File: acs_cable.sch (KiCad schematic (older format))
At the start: 0 parts

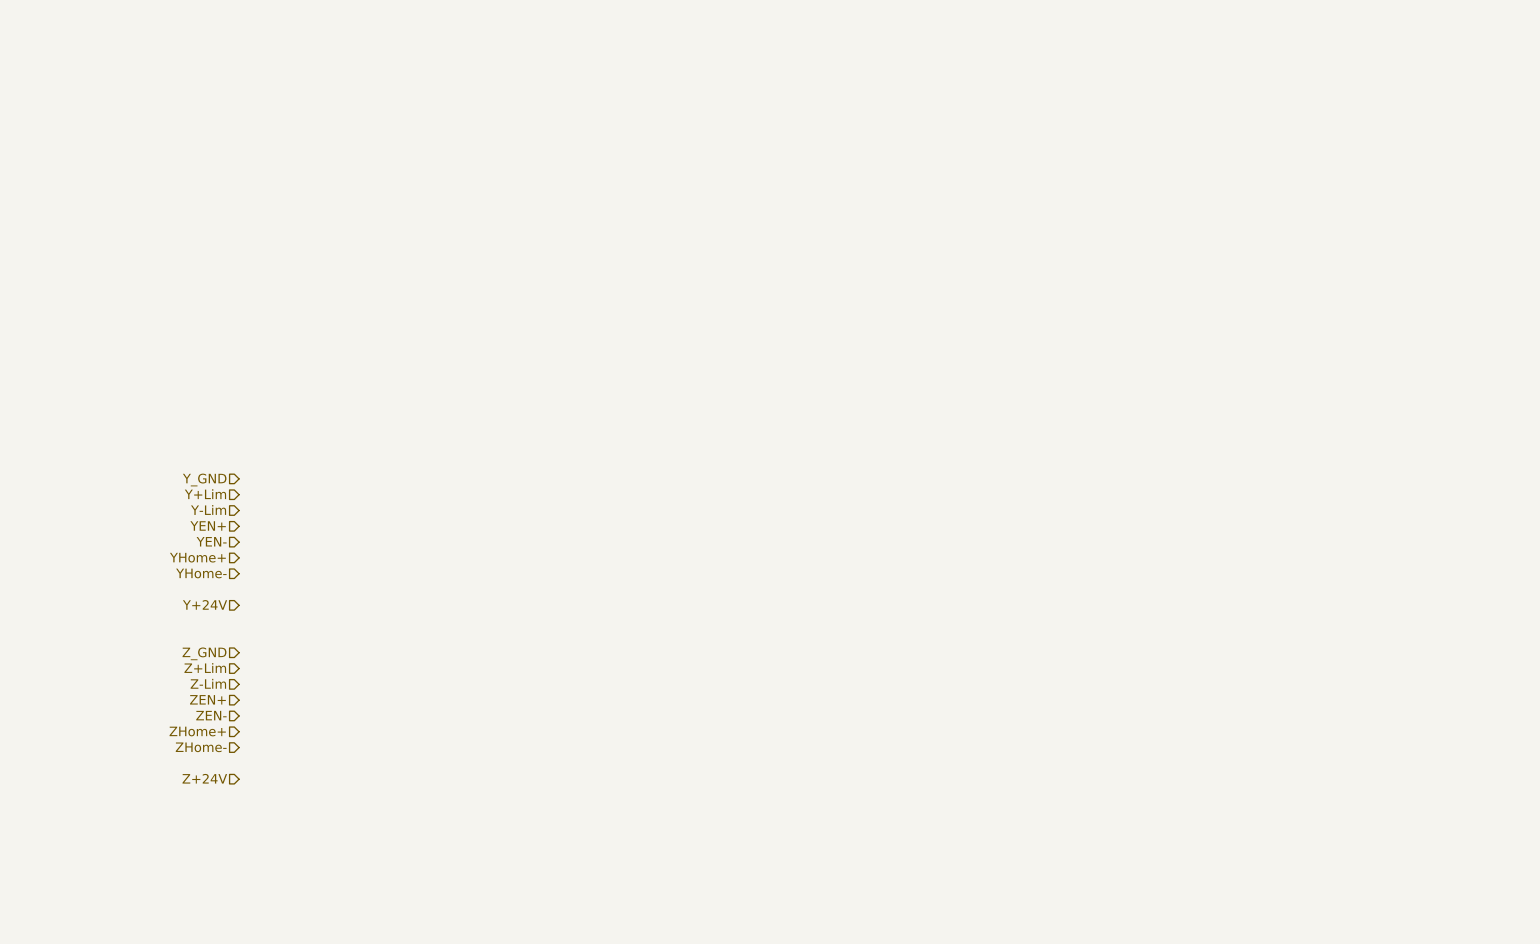
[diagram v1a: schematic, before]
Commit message: set limits to pull down, optional invert
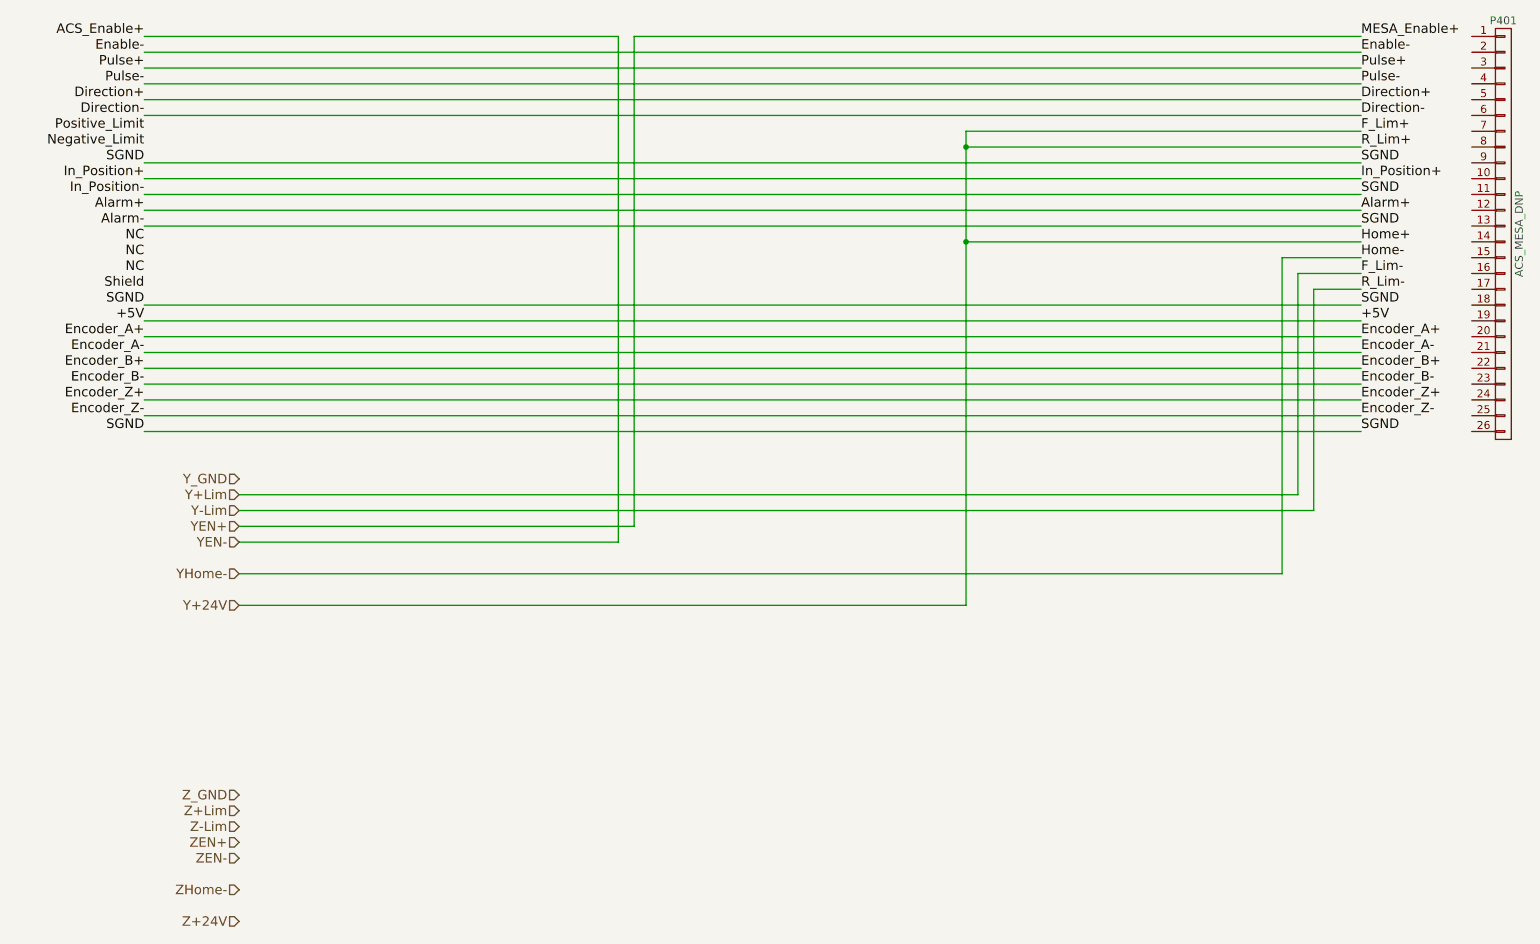
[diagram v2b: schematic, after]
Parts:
- added P401: ACS_MESA_DNP, symbol CONN_01X26
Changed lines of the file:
@@
 Text HLabel 2600 4400 0    60   Input ~ 0
 YEN-
-Text HLabel 2600 4500 0    60   Input ~ 0
-YHome+
 Text HLabel 2600 4600 0    60   Input ~ 0
 YHome-
 Text HLabel 2600 4800 0    60   Input ~ 0
 Y+24V
-Text HLabel 2600 5100 0    60   Input ~ 0
+Text HLabel 2600 6000 0    60   Input ~ 0
 Z_GND
-Text HLabel 2600 5200 0    60   Input ~ 0
+Text HLabel 2600 6100 0    60   Input ~ 0
 Z+Lim
-Text HLabel 2600 5300 0    60   Input ~ 0
+Text HLabel 2600 6200 0    60   Input ~ 0
 Z-Lim
-Text HLabel 2600 5400 0    60   Input ~ 0
+Text HLabel 2600 6300 0    60   Input ~ 0
 ZEN+
-Text HLabel 2600 5500 0    60   Input ~ 0
+Text HLabel 2600 6400 0    60   Input ~ 0
 ZEN-
-Text HLabel 2600 5600 0    60   Input ~ 0
-ZHome+
-Text HLabel 2600 5700 0    60   Input ~ 0
+Text HLabel 2600 6600 0    60   Input ~ 0
 ZHome-
-Text HLabel 2600 5900 0    60   Input ~ 0
+Text HLabel 2600 6800 0    60   Input ~ 0
 Z+24V
+Text Label 9700 1200 0    60   ~ 0
+MESA_Enable+
+Text Label 9700 1300 0    60   ~ 0
+Enable-
+Text Label 9700 1400 0    60   ~ 0
+Pulse+
+Text Label 9700 1500 0    60   ~ 0
+Pulse-
+Text Label 9700 1600 0    60   ~ 0
+Direction+
+Text Label 9700 1700 0    60   ~ 0
+Direction-
+Text Label 9700 1800 0    60   ~ 0
+F_Lim+
+Text Label 9700 1900 0    60   ~ 0
+R_Lim+
+Text Label 9700 2000 0    60   ~ 0
+SGND
+Text Label 9700 2100 0    60   ~ 0
+In_Position+
+Text Label 9700 2200 0    60   ~ 0
+SGND
+Text Label 9700 2300 0    60   ~ 0
+Alarm+
+Text Label 9700 2400 0    60   ~ 0
+SGND
+Text Label 9700 2500 0    60   ~ 0
+Home+
+Text Label 9700 2600 0    60   ~ 0
+Home-
+Text Label 9700 2700 0    60   ~ 0
+F_Lim-
+Text Label 9700 2800 0    60   ~ 0
+R_Lim-
+Text Label 9700 2900 0    60   ~ 0
+SGND
+Text Label 9700 3000 0    60   ~ 0
++5V
+Text Label 9700 3100 0    60   ~ 0
+Encoder_A+
+Text Label 9700 3200 0    60   ~ 0
+Encoder_A-
+Text Label 9700 3300 0    60   ~ 0
+Encoder_B+
+Text Label 9700 3400 0    60   ~ 0
+Encoder_B-
+Text Label 9700 3500 0    60   ~ 0
+Encoder_Z+
+Text Label 9700 3600 0    60   ~ 0
+Encoder_Z-
+Text Label 9700 3700 0    60   ~ 0
+SGND
+Text Label 2000 1200 2    60   ~ 0
+ACS_Enable+
+Text Label 2000 1300 2    60   ~ 0
+Enable-
+Text Label 2000 1400 2    60   ~ 0
+Pulse+
+Text Label 2000 1500 2    60   ~ 0
+Pulse-
+Text Label 2000 1600 2    60   ~ 0
+Direction+
+Text Label 2000 1700 2    60   ~ 0
+Direction-
+Text Label 2000 1800 2    60   ~ 0
+Positive_Limit
+Text Label 2000 1900 2    60   ~ 0
+Negative_Limit
+Text Label 2000 2000 2    60   ~ 0
+SGND
+Text Label 2000 2100 2    60   ~ 0
+In_Position+
+Text Label 2000 2200 2    60   ~ 0
+In_Position-
+Text Label 2000 2300 2    60   ~ 0
+Alarm+
+Text Label 2000 2400 2    60   ~ 0
+Alarm-
+Text Label 2000 2900 2    60   ~ 0
+SGND
+Text Label 2000 3000 2    60   ~ 0
++5V
+Text Label 2000 3100 2    60   ~ 0
+Encoder_A+
+Text Label 2000 3200 2    60   ~ 0
+Encoder_A-
+Text Label 2000 3300 2    60   ~ 0
+Encoder_B+
+Text Label 2000 3400 2    60   ~ 0
+Encoder_B-
+Text Label 2000 3500 2    60   ~ 0
+Encoder_Z+
+Text Label 2000 3600 2    60   ~ 0
+Encoder_Z-
+Text Label 2000 3700 2    60   ~ 0
+SGND
+Text Label 2000 2500 2    60   ~ 0
+NC
+Text Label 2000 2600 2    60   ~ 0
+NC
+Text Label 2000 2700 2    60   ~ 0
+NC
+Text Label 2000 2800 2    60   ~ 0
+Shield
+Wire Wire Line
+	2000 1400 9700 1400
+Wire Wire Line
+	9700 1500 2000 1500
+Wire Wire Line
+	2000 1600 9700 1600
+Wire Wire Line
+	9700 1700 2000 1700
+Wire Wire Line
+	2000 1300 9700 1300
+Wire Wire Line
+	2000 1200 5000 1200
+Wire Wire Line
+	5100 1200 9700 1200
+Wire Wire Line
+	2600 4400 5000 4400
+Wire Wire Line
+	5000 4400 5000 1200
+Wire Wire Line
+	2600 4300 5100 4300
+Wire Wire Line
+	5100 4300 5100 1200
+Wire Wire Line
+	2000 2000 9700 2000
+Wire Wire Line
+	9700 2100 2000 2100
+Wire Wire Line
+	2000 2200 9700 2200
+Wire Wire Line
+	9700 2300 2000 2300
+Wire Wire Line
+	2000 2400 9700 2400
+Wire Wire Line
+	9700 2600 9200 2600
+Wire Wire Line
+	9200 2600 9200 4600
+Wire Wire Line
+	9200 4600 2600 4600
+Wire Wire Line
+	9300 2700 9700 2700
+Wire Wire Line
+	2000 2900 9700 2900
+Wire Wire Line
+	9700 2800 9400 2800
+Wire Wire Line
+	9700 3000 2000 3000
+Wire Wire Line
+	2000 3100 9700 3100
+Wire Wire Line
+	9700 3200 2000 3200
+Wire Wire Line
+	2000 3300 9700 3300
+Wire Wire Line
+	9700 3400 2000 3400
+Wire Wire Line
+	2000 3500 9700 3500
+Wire Wire Line
+	9700 3600 2000 3600
+Wire Wire Line
+	2000 3700 9700 3700
+Wire Wire Line
+	2600 4100 9300 4100
+Wire Wire Line
+	2600 4200 9400 4200
+$Comp
+L CONN_01X26 P401
+U 1 1 57C02ACE
+P 10600 2450
+F 0 "P401" H 10600 3800 50  0000 C CNN
+F 1 "ACS_MESA_DNP" V 10700 2450 50  0000 C CNN
+F 2 "" H 10600 2450 50  0001 C CNN
+F 3 "" H 10600 2450 50  0000 C CNN
+	1    10600 2450
+	1    0    0    -1
+$EndComp
+Wire Wire Line
+	7200 4800 2600 4800
+Wire Wire Line
+	7200 1800 7200 4800
+Wire Wire Line
+	7200 2500 9700 2500
+Wire Wire Line
+	7200 1800 9700 1800
+Connection ~ 7200 2500
+Wire Wire Line
+	9700 1900 7200 1900
+Connection ~ 7200 1900
+Wire Wire Line
+	9400 4200 9400 2800
+Wire Wire Line
+	9300 4100 9300 2700
 $EndSCHEMATC

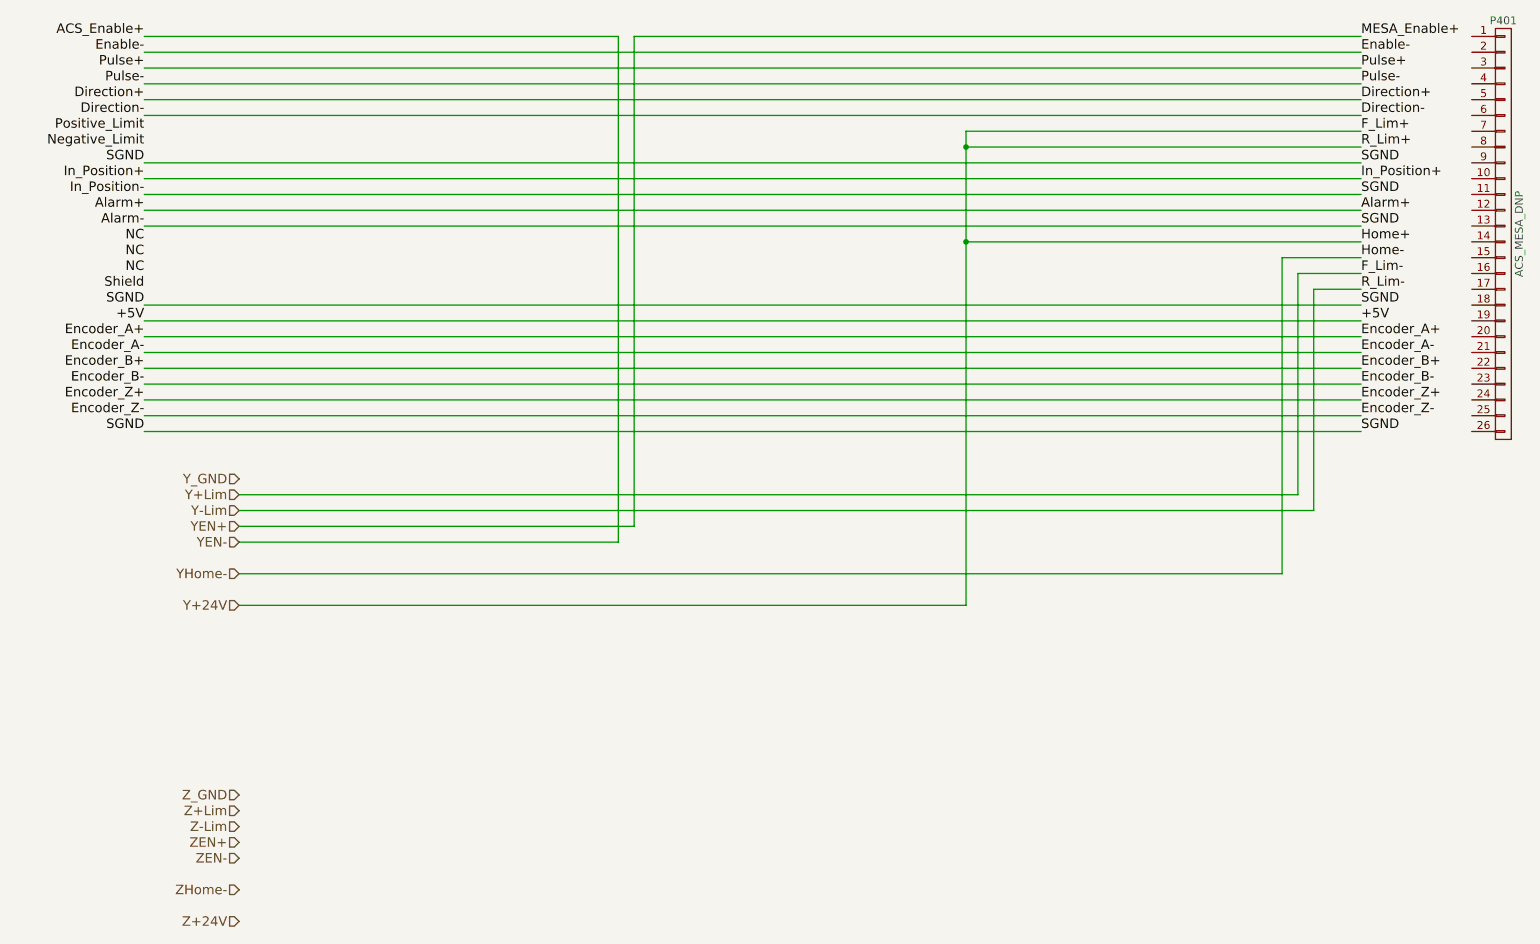
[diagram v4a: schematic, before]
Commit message: checked limits and homes, removed enable, adjusted routing
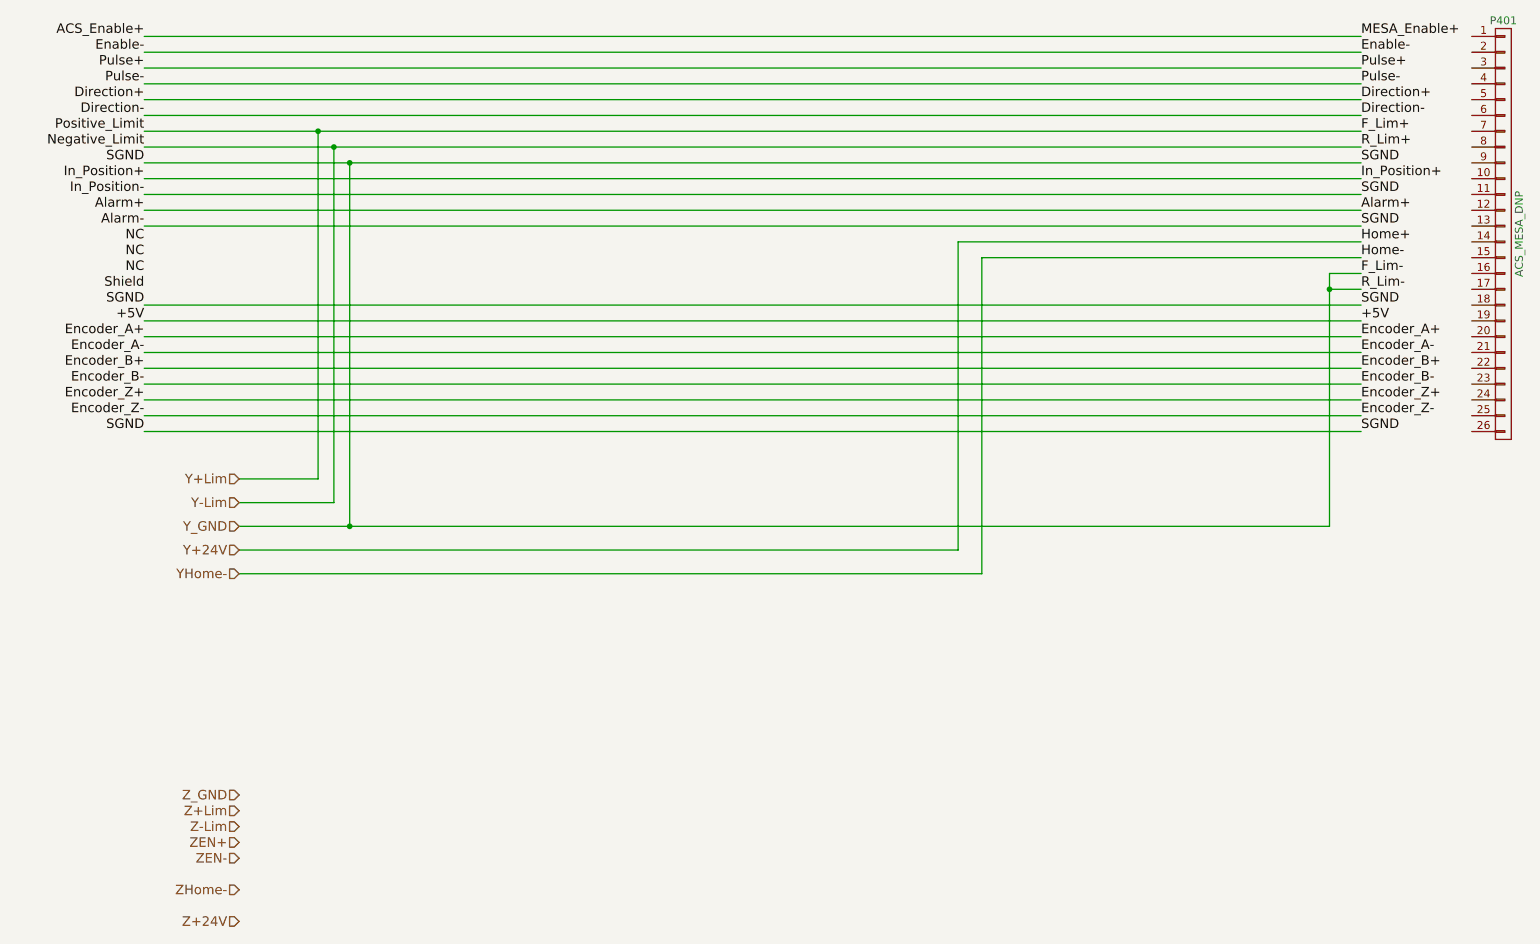
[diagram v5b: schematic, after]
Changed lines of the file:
@@
 $Descr A4 11693 8268
 encoding utf-8
-Sheet 5 5
+Sheet 4 4
 Title ""
 Date ""
@@
 Comment4 ""
 $EndDescr
+Text HLabel 2600 4300 0    60   Input ~ 0
+Y_GND
 Text HLabel 2600 4000 0    60   Input ~ 0
-Y_GND
-Text HLabel 2600 4100 0    60   Input ~ 0
 Y+Lim
-Text HLabel 2600 4200 0    60   Input ~ 0
+Text HLabel 2600 4150 0    60   Input ~ 0
 Y-Lim
-Text HLabel 2600 4300 0    60   Input ~ 0
-YEN+
-Text HLabel 2600 4400 0    60   Input ~ 0
-YEN-
 Text HLabel 2600 4600 0    60   Input ~ 0
 YHome-
-Text HLabel 2600 4800 0    60   Input ~ 0
+Text HLabel 2600 4450 0    60   Input ~ 0
 Y+24V
 Text HLabel 2600 6000 0    60   Input ~ 0
@@
 Text Label 2000 2800 2    60   ~ 0
 Shield
-Wire Wire Line
-	2000 1400 9700 1400
-Wire Wire Line
-	9700 1500 2000 1500
-Wire Wire Line
-	2000 1600 9700 1600
-Wire Wire Line
-	9700 1700 2000 1700
-Wire Wire Line
-	2000 1300 9700 1300
-Wire Wire Line
-	2000 1200 5000 1200
-Wire Wire Line
-	5100 1200 9700 1200
-Wire Wire Line
-	2600 4400 5000 4400
-Wire Wire Line
-	5000 4400 5000 1200
-Wire Wire Line
-	2600 4300 5100 4300
-Wire Wire Line
-	5100 4300 5100 1200
-Wire Wire Line
-	2000 2000 9700 2000
-Wire Wire Line
-	9700 2100 2000 2100
-Wire Wire Line
-	2000 2200 9700 2200
-Wire Wire Line
-	9700 2300 2000 2300
-Wire Wire Line
-	2000 2400 9700 2400
-Wire Wire Line
-	9700 2600 9200 2600
-Wire Wire Line
-	9200 2600 9200 4600
-Wire Wire Line
-	9200 4600 2600 4600
-Wire Wire Line
-	9300 2700 9700 2700
-Wire Wire Line
-	2000 2900 9700 2900
-Wire Wire Line
-	9700 2800 9400 2800
-Wire Wire Line
-	9700 3000 2000 3000
-Wire Wire Line
-	2000 3100 9700 3100
-Wire Wire Line
-	9700 3200 2000 3200
-Wire Wire Line
-	2000 3300 9700 3300
-Wire Wire Line
-	9700 3400 2000 3400
-Wire Wire Line
-	2000 3500 9700 3500
-Wire Wire Line
-	9700 3600 2000 3600
-Wire Wire Line
-	2000 3700 9700 3700
-Wire Wire Line
-	2600 4100 9300 4100
-Wire Wire Line
-	2600 4200 9400 4200
 $Comp
 L CONN_01X26 P401
@@
 $EndComp
 Wire Wire Line
-	7200 4800 2600 4800
-Wire Wire Line
-	7200 1800 7200 4800
-Wire Wire Line
-	7200 2500 9700 2500
-Wire Wire Line
-	7200 1800 9700 1800
-Connection ~ 7200 2500
-Wire Wire Line
-	9700 1900 7200 1900
-Connection ~ 7200 1900
-Wire Wire Line
-	9400 4200 9400 2800
-Wire Wire Line
-	9300 4100 9300 2700
+	2600 4150 3200 4150
+Wire Wire Line
+	3100 4000 2600 4000
+Wire Wire Line
+	7150 2500 7150 4450
+Connection ~ 3200 1900
+Connection ~ 3100 1800
+Wire Wire Line
+	2000 1900 9700 1900
+Wire Wire Line
+	3200 4150 3200 1900
+Wire Wire Line
+	3100 1800 3100 4000
+Wire Wire Line
+	2000 1800 9700 1800
+Wire Wire Line
+	7150 2500 9700 2500
+Wire Wire Line
+	7150 4450 2600 4450
+Wire Wire Line
+	2000 3700 9700 3700
+Wire Wire Line
+	9700 3600 2000 3600
+Wire Wire Line
+	2000 3500 9700 3500
+Wire Wire Line
+	9700 3400 2000 3400
+Wire Wire Line
+	2000 3300 9700 3300
+Wire Wire Line
+	9700 3200 2000 3200
+Wire Wire Line
+	2000 3100 9700 3100
+Wire Wire Line
+	9700 3000 2000 3000
+Wire Wire Line
+	2000 2900 9700 2900
+Wire Wire Line
+	7300 4600 2600 4600
+Wire Wire Line
+	7300 2600 7300 4600
+Wire Wire Line
+	9700 2600 7300 2600
+Wire Wire Line
+	2000 2400 9700 2400
+Wire Wire Line
+	9700 2300 2000 2300
+Wire Wire Line
+	2000 2200 9700 2200
+Wire Wire Line
+	9700 2100 2000 2100
+Wire Wire Line
+	2000 2000 9700 2000
+Wire Wire Line
+	2000 1200 9700 1200
+Wire Wire Line
+	2000 1300 9700 1300
+Wire Wire Line
+	9700 1700 2000 1700
+Wire Wire Line
+	2000 1600 9700 1600
+Wire Wire Line
+	9700 1500 2000 1500
+Wire Wire Line
+	2000 1400 9700 1400
+Wire Wire Line
+	9500 4300 2600 4300
+Wire Wire Line
+	9500 2700 9500 4300
+Wire Wire Line
+	9500 2700 9700 2700
+Wire Wire Line
+	9700 2800 9500 2800
+Connection ~ 9500 2800
+Wire Wire Line
+	3300 2000 3300 4300
+Connection ~ 3300 4300
+Connection ~ 3300 2000
 $EndSCHEMATC
